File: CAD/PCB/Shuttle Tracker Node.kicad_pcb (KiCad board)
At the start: 2 copper layers, 98.9 x 44.1 mm, 27 parts, among them J1 Conn_01x01, J2 Conn_01x01, J3 Conn_01x01, J4 Conn_01x01, J5 Conn_01x01, J6 Conn_01x01, J7 Conn_01x01, SW1 SW_Push, SW10 SW_Push, SW11 SW_Push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

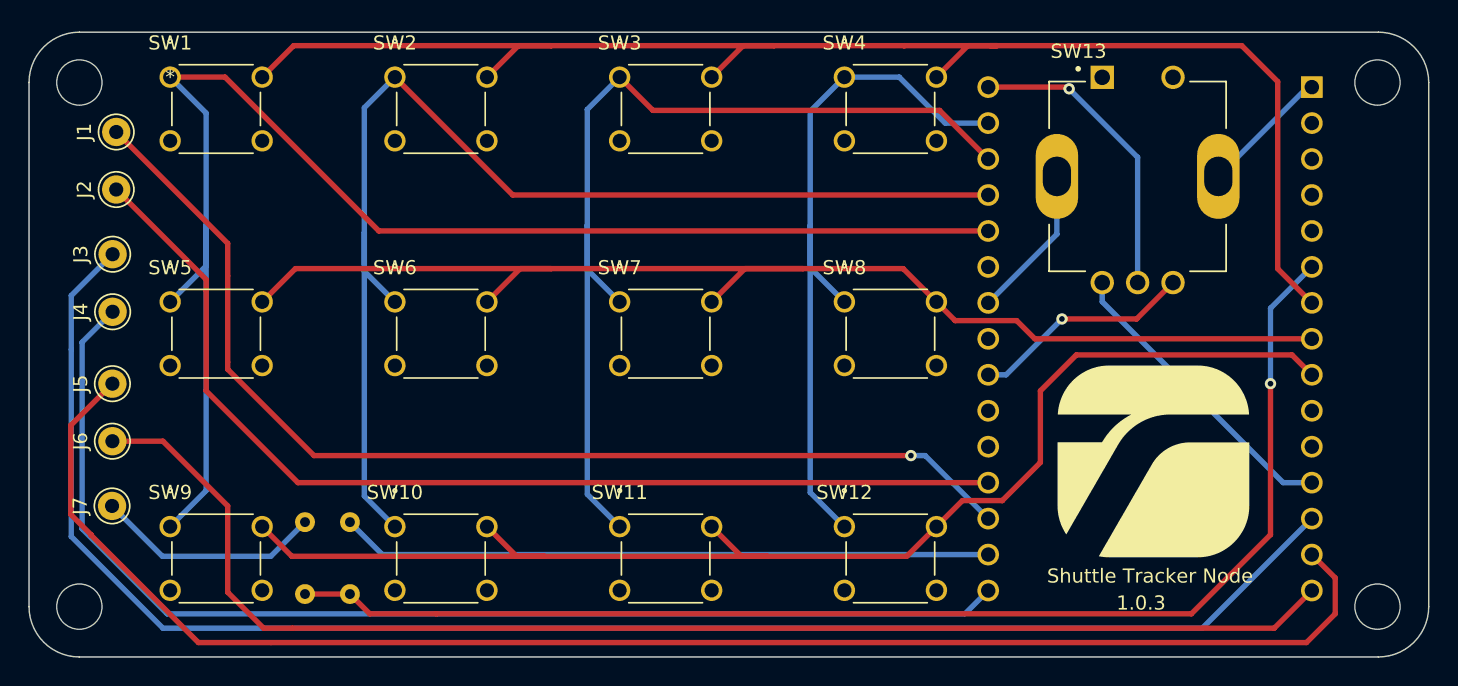
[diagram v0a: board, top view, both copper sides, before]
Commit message: Fixed trace and mounting hole overlap
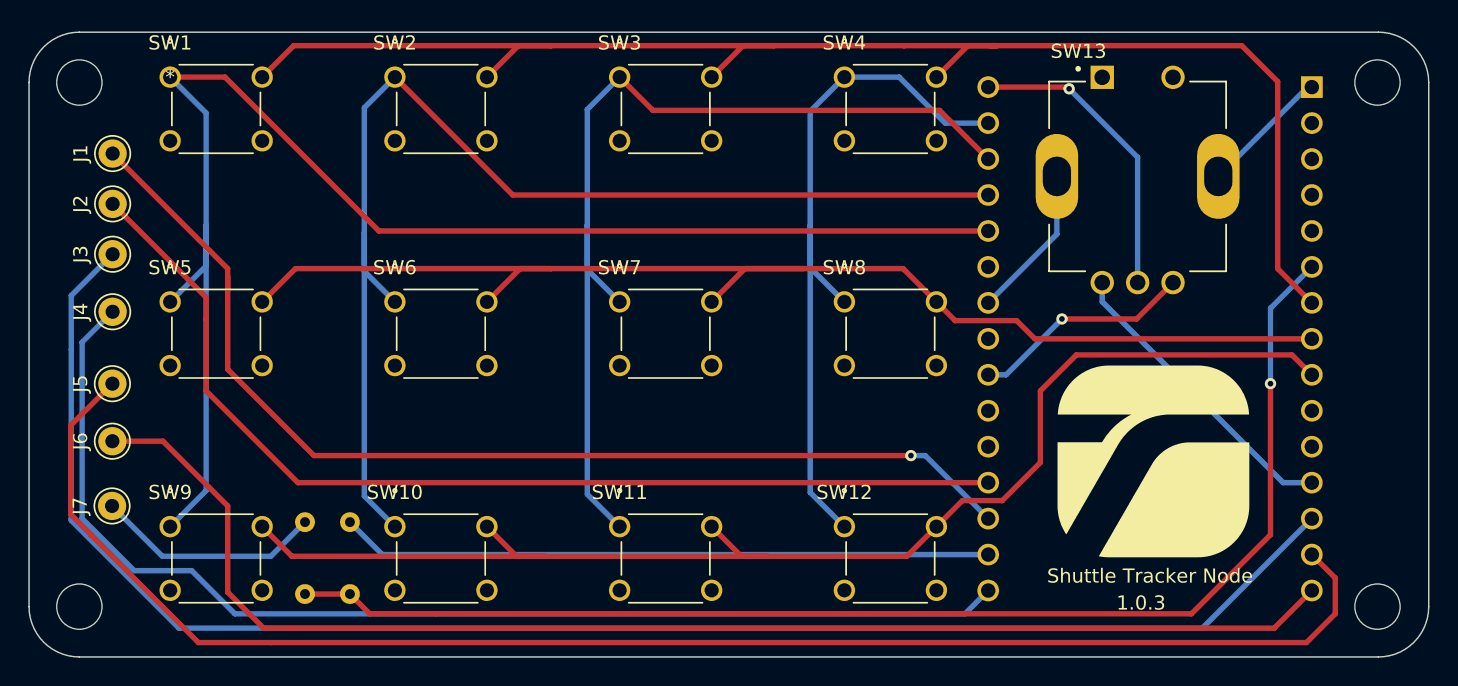
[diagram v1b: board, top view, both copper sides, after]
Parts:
- moved J1 1.55 mm to (135.6, 86.4)
- moved J2 1.05 mm to (135.6, 89.9)
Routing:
- net LCD_CLK: track 74.8 -> 73.9 mm
- net LCD_5V: track 114.7 -> 114.0 mm
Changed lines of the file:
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@@
   )
   (footprint "Connector_Pin:Pin_D1.0mm_L10.0mm" (layer "F.Cu")
-    (at 135.89 88.9 -90)
+    (at 135.636 89.916 -90)
     (descr "solder Pin_ diameter 1.0mm, hole diameter 1.0mm (press fit), length 10.0mm")
     (tags "solder Pin_ press fit")
@@
   )
   (footprint "Connector_Pin:Pin_D1.0mm_L10.0mm" (layer "F.Cu")
-    (at 135.89 84.836 -90)
+    (at 135.636 86.36 -90)
     (descr "solder Pin_ diameter 1.0mm, hole diameter 1.0mm (press fit), length 10.0mm")
     (tags "solder Pin_ press fit")
@@
     (effects (font (size 1 1) (thickness 0.15)))
   )
-  (segment (start 143.764 94.996) (end 143.764 101.092) (width 0.381) (layer "F.Cu") (net 1))
+  (segment (start 143.764 94.488) (end 143.764 96.012) (width 0.381) (layer "F.Cu") (net 1))
   (segment (start 149.86 107.696) (end 192.024 107.696) (width 0.381) (layer "F.Cu") (net 1))
   (segment (start 143.764 101.092) (end 143.764 101.6) (width 0.381) (layer "F.Cu") (net 1))
-  (segment (start 135.89 84.836) (end 143.764 92.71) (width 0.381) (layer "F.Cu") (net 1))
   (segment (start 143.764 101.6) (end 149.86 107.696) (width 0.381) (layer "F.Cu") (net 1))
-  (segment (start 143.764 92.71) (end 143.764 94.996) (width 0.381) (layer "F.Cu") (net 1))
+  (segment (start 143.764 94.996) (end 143.764 96.012) (width 0.381) (layer "F.Cu") (net 1))
+  (segment (start 143.764 96.012) (end 143.764 101.092) (width 0.381) (layer "F.Cu") (net 1))
+  (segment (start 135.636 86.36) (end 143.764 94.488) (width 0.381) (layer "F.Cu") (net 1))
   (via (at 192.024 107.696) (size 0.8) (drill 0.4) (layers "F.Cu" "B.Cu") (net 1))
   (segment (start 192.024 107.696) (end 193.0332 107.696) (width 0.381) (layer "B.Cu") (net 1))
   (segment (start 193.0332 107.696) (end 197.485 112.1478) (width 0.381) (layer "B.Cu") (net 1))
-  (segment (start 142.24 95.25) (end 142.24 96.012) (width 0.381) (layer "F.Cu") (net 2))
-  (segment (start 142.24 103.124) (end 142.24 96.012) (width 0.381) (layer "F.Cu") (net 2))
   (segment (start 197.485 109.6078) (end 148.7238 109.6078) (width 0.381) (layer "F.Cu") (net 2))
+  (segment (start 142.24 96.52) (end 142.24 98.044) (width 0.381) (layer "F.Cu") (net 2))
   (segment (start 148.7238 109.6078) (end 142.24 103.124) (width 0.381) (layer "F.Cu") (net 2))
-  (segment (start 135.89 88.9) (end 142.24 95.25) (width 0.381) (layer "F.Cu") (net 2))
+  (segment (start 135.636 89.916) (end 142.24 96.52) (width 0.381) (layer "F.Cu") (net 2))
+  (segment (start 142.24 103.124) (end 142.24 98.044) (width 0.381) (layer "F.Cu") (net 2))
+  (segment (start 132.713091 112.275117) (end 140.325974 119.888) (width 0.381) (layer "B.Cu") (net 3))
+  (segment (start 140.325974 119.888) (end 212.6048 119.888) (width 0.381) (layer "B.Cu") (net 3))
+  (segment (start 132.713091 100.201091) (end 132.713091 112.142909) (width 0.381) (layer "B.Cu") (net 3))
+  (segment (start 132.713091 96.394909) (end 132.713091 100.201091) (width 0.381) (layer "B.Cu") (net 3))
+  (segment (start 132.713091 112.142909) (end 132.713091 112.275117) (width 0.381) (layer "B.Cu") (net 3))
+  (segment (start 135.636 93.472) (end 132.713091 96.394909) (width 0.381) (layer "B.Cu") (net 3))
   (segment (start 212.6048 119.888) (end 220.345 112.1478) (width 0.381) (layer "B.Cu") (net 3))
-  (segment (start 132.713091 113.409091) (end 139.192 119.888) (width 0.381) (layer "B.Cu") (net 3))
-  (segment (start 139.192 119.888) (end 212.6048 119.888) (width 0.381) (layer "B.Cu") (net 3))
-  (segment (start 132.713091 96.394909) (end 132.713091 100.201091) (width 0.381) (layer "B.Cu") (net 3))
-  (segment (start 132.713091 100.201091) (end 132.713091 113.409091) (width 0.381) (layer "B.Cu") (net 3))
-  (segment (start 135.636 93.472) (end 132.713091 96.394909) (width 0.381) (layer "B.Cu") (net 3))
-  (segment (start 133.475091 102.487091) (end 133.475091 112.862131) (width 0.381) (layer "B.Cu") (net 4))
-  (segment (start 135.636 97.536) (end 133.475091 99.696909) (width 0.381) (layer "B.Cu") (net 4))
-  (segment (start 133.475091 99.696909) (end 133.475091 102.487091) (width 0.381) (layer "B.Cu") (net 4))
-  (segment (start 133.475091 112.862131) (end 139.48496 118.872) (width 0.381) (layer "B.Cu") (net 4))
+  (segment (start 144.272 118.872) (end 195.8408 118.872) (width 0.381) (layer "B.Cu") (net 4))
+  (segment (start 141.224 115.824) (end 137.16 115.824) (width 0.381) (layer "B.Cu") (net 4))
+  (segment (start 144.272 118.872) (end 141.224 115.824) (width 0.381) (layer "B.Cu") (net 4))
+  (segment (start 133.475091 99.696909) (end 135.636 97.536) (width 0.381) (layer "B.Cu") (net 4))
+  (segment (start 137.16 115.824) (end 133.475091 112.139091) (width 0.381) (layer "B.Cu") (net 4))
+  (segment (start 133.475091 112.139091) (end 133.475091 99.696909) (width 0.381) (layer "B.Cu") (net 4))
   (segment (start 195.8408 118.872) (end 197.485 117.2278) (width 0.381) (layer "B.Cu") (net 4))
-  (segment (start 139.48496 118.872) (end 195.8408 118.872) (width 0.381) (layer "B.Cu") (net 4))
   (segment (start 143.57454 80.9625) (end 139.7 80.9625) (width 0.381) (layer "F.Cu") (net 5))
   (segment (start 197.485 91.8278) (end 154.43984 91.8278) (width 0.381) (layer "F.Cu") (net 5))

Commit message: Updated pin configuration for buttons
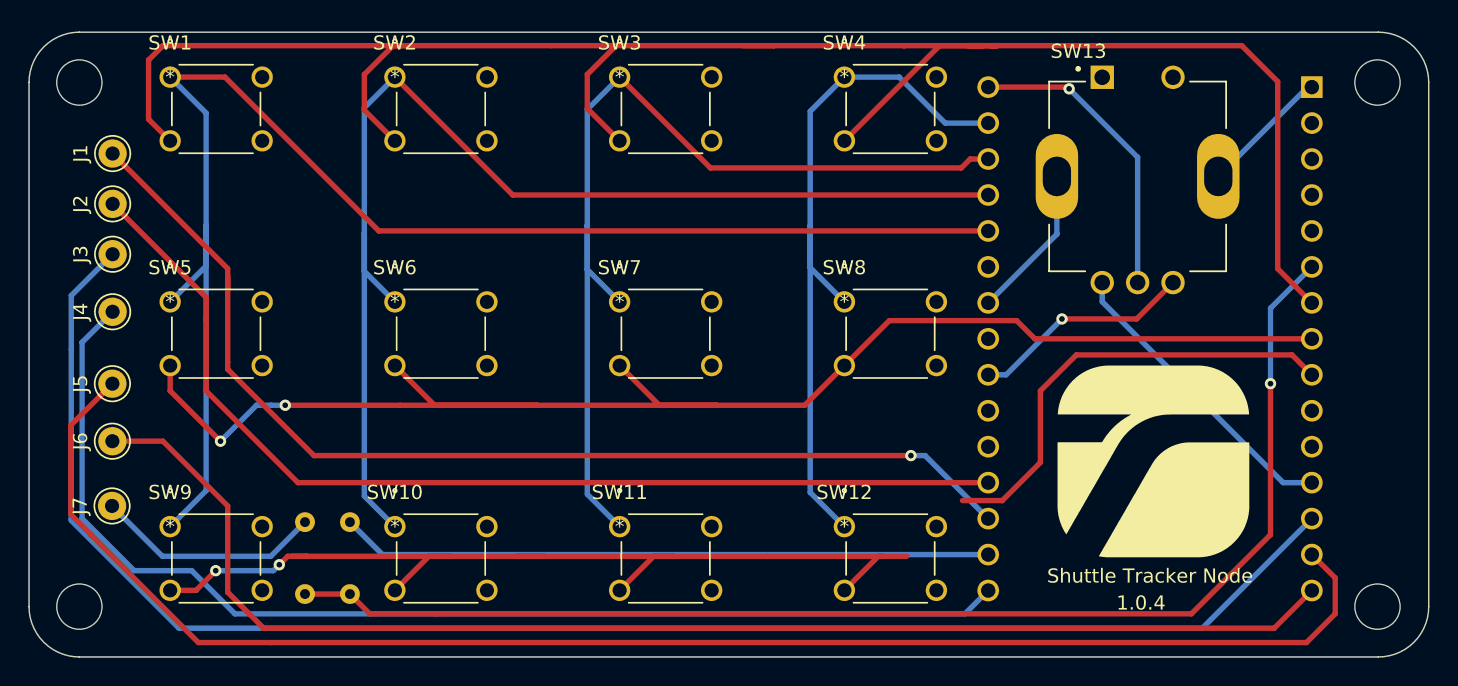
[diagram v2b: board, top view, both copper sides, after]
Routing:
- net R1: track 107.0 -> 140.1 mm
- net R2: track 90.1 -> 107.2 mm, vias 0 -> 2
- net R3: track 94.1 -> 101.9 mm, vias 0 -> 2
- net C3: track 68.4 -> 68.9 mm
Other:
- board text added: "1.0.4"
- board text removed: "1.0.3"

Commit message: Updated pin congifuration again
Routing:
- net R1: track 140.1 -> 110.6 mm
- net R2: track 107.2 -> 86.1 mm, vias 2 -> 0
- net R3: track 101.9 -> 93.4 mm, vias 2 -> 0
- net C4: track 51.7 -> 54.0 mm, vias 0 -> 1
- net C2: track 84.7 -> 86.8 mm
- net C1: track 102.6 -> 101.2 mm, vias 0 -> 1
- net V_GND: track 46.0 -> 46.9 mm
- net C3: track 68.9 -> 68.2 mm, vias 0 -> 1
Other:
- board text added: "1.0.5"
- board text removed: "1.0.4"
